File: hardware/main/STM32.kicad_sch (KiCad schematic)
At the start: 36 parts, among them U201 REF3430QDGKRQ1, U202 STM32L431RCTx

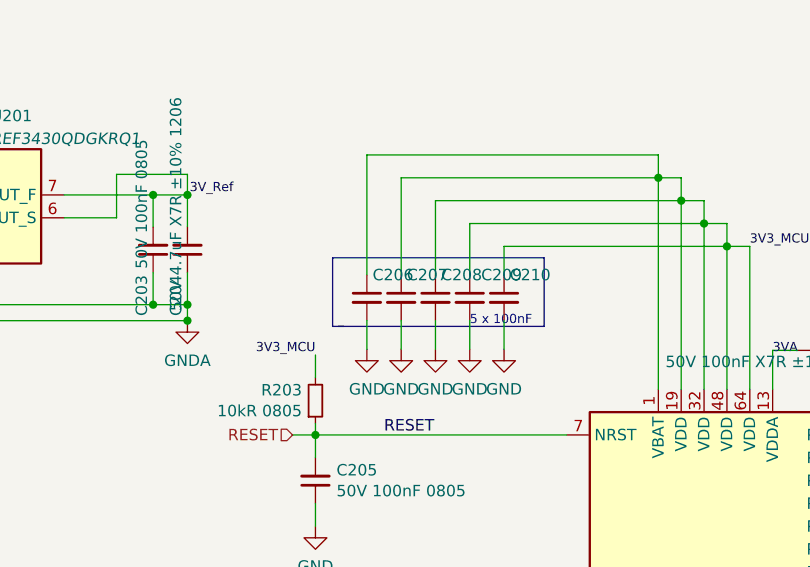
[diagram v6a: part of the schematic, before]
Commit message: Layout: Fist version of power stage
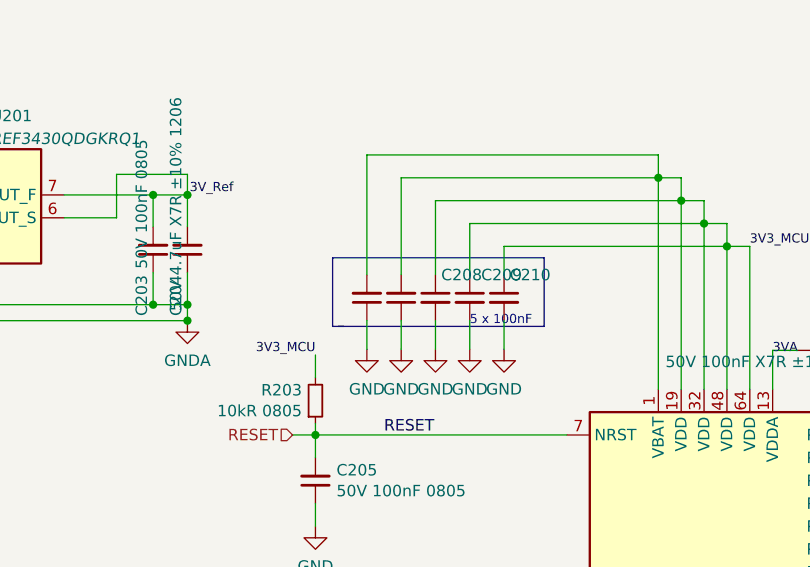
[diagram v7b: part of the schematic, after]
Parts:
- C206, C207: value 50V 100nF X7R ±10% 0402 -> 50V 100nF 0805; footprint Capacitor_SMD:C_0402_1005Metric_Pad0.74x0.62mm_HandSolder -> Capacitor_SMD:C_0805_2012Metric_Pad1.18x1.45mm_HandSolder
- JP201, JP202, JP204, JP205, JP206, JP207: footprint Jumper:SolderJumper-2_P1.3mm_Open_TrianglePad1.0x1.5mm -> Zenite:SolderJumper-2_P0.5mm_Open_TrianglePad0.5x0.5mm
- JP203: footprint Jumper:SolderJumper-3_P1.3mm_Open_Pad1.0x1.5mm -> Jumper:SolderJumper-3_P2.0mm_Open_TrianglePad1.0x1.5mm
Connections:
- net 3V3_MCU: now also C206.2, C207.2; no longer C206.1, C207.1
- net GND: now also C206.1, C207.1; no longer C206.2, C207.2
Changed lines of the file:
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@@
       (effects (font (size 1 1)))
     )
-    (property "Footprint" "Jumper:SolderJumper-2_P1.3mm_Open_TrianglePad1.0x1.5mm" (id 2) (at 167.64 142.24 0)
+    (property "Footprint" "Zenite:SolderJumper-2_P0.5mm_Open_TrianglePad0.5x0.5mm" (id 2) (at 167.64 142.24 0)
       (effects (font (size 1.27 1.27)) hide)
     )
@@
     (property "Reference" "JP202" (id 0) (at 241.3 18.5252 0))
     (property "Value" "Enable Voltage Reference" (id 1) (at 241.3 21.0621 0))
-    (property "Footprint" "Jumper:SolderJumper-2_P1.3mm_Open_TrianglePad1.0x1.5mm" (id 2) (at 241.3 22.86 0)
+    (property "Footprint" "Zenite:SolderJumper-2_P0.5mm_Open_TrianglePad0.5x0.5mm" (id 2) (at 241.3 22.86 0)
       (effects (font (size 1.27 1.27)) hide)
     )
     (property "Datasheet" "~" (id 3) (at 241.3 22.86 0)
-      (effects (font (size 1.27 1.27)) hide)
-    )
-    (pin "1")
-    (pin "2")
-  )
-  (symbol (lib_id "Device:C_Small") (at 100.33 60.96 0) (unit 1)
-    (in_bom yes) (on_board yes)
-    (property "Reference" "C206" (id 0) (at 100.965 58.42 0)
-      (effects (font (size 1.27 1.27)) (justify left))
-    )
-    (property "Value" "50V 100nF X7R ±10% 0402" (id 1) (at 102.7811 62.6685 0)
-      (effects (font (size 1.27 1.27)) (justify left) hide)
-    )
-    (property "Footprint" "Capacitor_SMD:C_0402_1005Metric_Pad0.74x0.62mm_HandSolder" (id 2) (at 100.33 60.96 0)
-      (effects (font (size 1.27 1.27)) hide)
-    )
-    (property "Datasheet" "~" (id 3) (at 100.33 60.96 0)
       (effects (font (size 1.27 1.27)) hide)
     )
@@
     (property "Reference" "JP201" (id 0) (at 240.03 45.8302 0))
     (property "Value" "Enable Stm32 Supply" (id 1) (at 240.03 48.3671 0))
-    (property "Footprint" "Jumper:SolderJumper-2_P1.3mm_Open_TrianglePad1.0x1.5mm" (id 2) (at 240.03 50.165 0)
+    (property "Footprint" "Zenite:SolderJumper-2_P0.5mm_Open_TrianglePad0.5x0.5mm" (id 2) (at 240.03 50.165 0)
       (effects (font (size 1.27 1.27)) hide)
     )
@@
     )
     (property "Datasheet" "~" (id 3) (at 37.465 56.134 0)
+      (effects (font (size 1.27 1.27)) hide)
+    )
+    (pin "1")
+    (pin "2")
+  )
+  (symbol (lib_id "Device:C_Small") (at 104.14 60.96 180) (unit 1)
+    (in_bom yes) (on_board yes)
+    (property "Reference" "C207" (id 0) (at 106.4768 59.7916 0)
+      (effects (font (size 1.27 1.27)) (justify right) hide)
+    )
+    (property "Value" "50V 100nF 0805" (id 1) (at 106.4768 62.103 0)
+      (effects (font (size 1.27 1.27)) (justify right) hide)
+    )
+    (property "Footprint" "Capacitor_SMD:C_0805_2012Metric_Pad1.18x1.45mm_HandSolder" (id 2) (at 104.14 60.96 0)
+      (effects (font (size 1.27 1.27)) hide)
+    )
+    (property "Datasheet" "~" (id 3) (at 104.14 60.96 0)
       (effects (font (size 1.27 1.27)) hide)
     )
@@
     (pin "1")
   )
+  (symbol (lib_id "Device:C_Small") (at 100.33 60.96 180) (unit 1)
+    (in_bom yes) (on_board yes)
+    (property "Reference" "C206" (id 0) (at 102.6668 59.7916 0)
+      (effects (font (size 1.27 1.27)) (justify right) hide)
+    )
+    (property "Value" "50V 100nF 0805" (id 1) (at 102.6668 62.103 0)
+      (effects (font (size 1.27 1.27)) (justify right) hide)
+    )
+    (property "Footprint" "Capacitor_SMD:C_0805_2012Metric_Pad1.18x1.45mm_HandSolder" (id 2) (at 100.33 60.96 0)
+      (effects (font (size 1.27 1.27)) hide)
+    )
+    (property "Datasheet" "~" (id 3) (at 100.33 60.96 0)
+      (effects (font (size 1.27 1.27)) hide)
+    )
+    (pin "1")
+    (pin "2")
+  )
   (symbol (lib_id "power:GND") (at 205.74 165.735 0) (unit 1)
     (in_bom yes) (on_board yes) (fields_autoplaced)
@@
       (effects (font (size 1 1)))
     )
-    (property "Footprint" "Jumper:SolderJumper-2_P1.3mm_Open_TrianglePad1.0x1.5mm" (id 2) (at 167.64 137.16 0)
+    (property "Footprint" "Zenite:SolderJumper-2_P0.5mm_Open_TrianglePad0.5x0.5mm" (id 2) (at 167.64 137.16 0)
       (effects (font (size 1.27 1.27)) hide)
     )
@@
       (effects (font (size 1 1)))
     )
-    (property "Footprint" "Jumper:SolderJumper-2_P1.3mm_Open_TrianglePad1.0x1.5mm" (id 2) (at 167.64 139.7 0)
+    (property "Footprint" "Zenite:SolderJumper-2_P0.5mm_Open_TrianglePad0.5x0.5mm" (id 2) (at 167.64 139.7 0)
       (effects (font (size 1.27 1.27)) hide)
     )
@@
       (effects (font (size 1 1)))
     )
-    (property "Footprint" "Jumper:SolderJumper-2_P1.3mm_Open_TrianglePad1.0x1.5mm" (id 2) (at 167.64 134.62 0)
+    (property "Footprint" "Zenite:SolderJumper-2_P0.5mm_Open_TrianglePad0.5x0.5mm" (id 2) (at 167.64 134.62 0)
       (effects (font (size 1.27 1.27)) hide)
     )
@@
     (pin "1")
   )
-  (symbol (lib_id "Device:C_Small") (at 104.14 60.96 0) (unit 1)
-    (in_bom yes) (on_board yes)
-    (property "Reference" "C207" (id 0) (at 104.775 58.42 0)
-      (effects (font (size 1.27 1.27)) (justify left))
-    )
-    (property "Value" "50V 100nF X7R ±10% 0402" (id 1) (at 106.5911 62.6685 0)
-      (effects (font (size 1.27 1.27)) (justify left) hide)
-    )
-    (property "Footprint" "Capacitor_SMD:C_0402_1005Metric_Pad0.74x0.62mm_HandSolder" (id 2) (at 104.14 60.96 0)
-      (effects (font (size 1.27 1.27)) hide)
-    )
-    (property "Datasheet" "~" (id 3) (at 104.14 60.96 0)
-      (effects (font (size 1.27 1.27)) hide)
-    )
-    (pin "1")
-    (pin "2")
-  )
   (symbol (lib_id "Jumper:Jumper_3_Bridged12") (at 241.3 36.195 0) (unit 1)
     (in_bom yes) (on_board yes) (fields_autoplaced)
     (property "Reference" "JP203" (id 0) (at 241.3 31.631 0))
     (property "Value" "Analog_Ref" (id 1) (at 241.3 34.1679 0))
-    (property "Footprint" "Jumper:SolderJumper-3_P1.3mm_Open_Pad1.0x1.5mm" (id 2) (at 241.3 36.195 0)
-      (effects (font (size 1.27 1.27)) hide)
-    )
+    (property "Footprint" "Jumper:SolderJumper-3_P2.0mm_Open_TrianglePad1.0x1.5mm" (id 2) (at 241.3 36.195 0)
+      (effects (font (size 1.27 1.27)) hide)
+    )

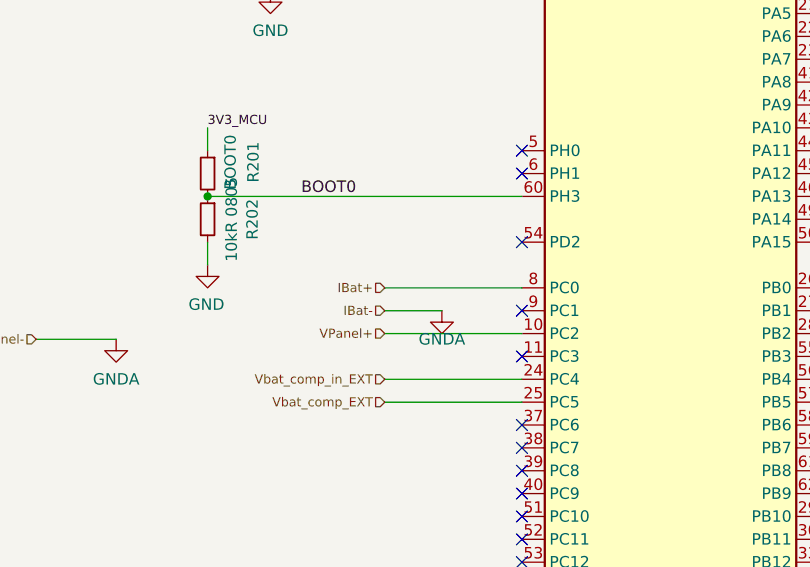
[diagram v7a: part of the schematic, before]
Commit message: Layout: Organize and initialize routing of control
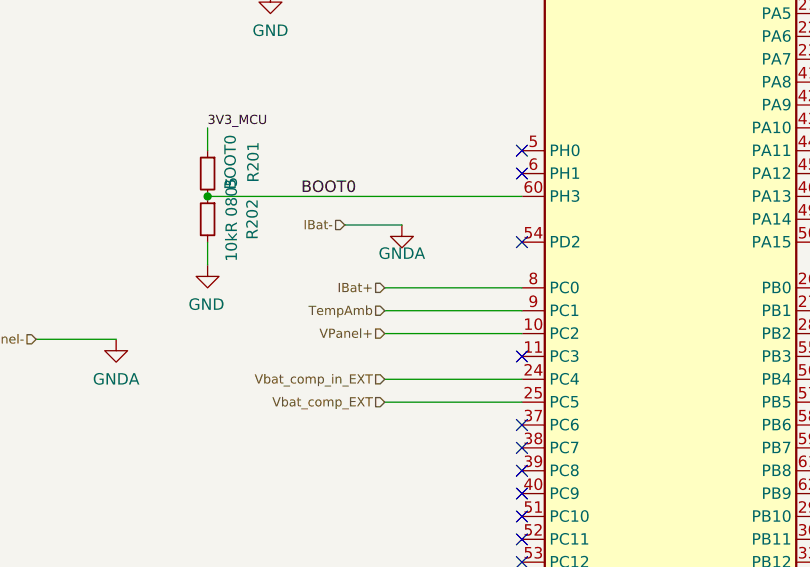
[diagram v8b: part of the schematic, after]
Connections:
- net TempAmb: now reaches U202.9 (PC1)
- no-connect marks 19 -> 18
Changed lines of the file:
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@@
   (junction (at 80.391 61.722) (diameter 0) (color 0 0 0 0)
   )
-  (no_connect (at 122.555 121.92))
   (no_connect (at 122.555 157.48))
   (no_connect (at 122.555 127))
@@
     (stroke (width 0) (type default) (color 0 0 0 0))
   )
-  (wire (pts (xy 107.315 121.92) (xy 113.665 121.92))
+  (wire (pts (xy 102.87 112.395) (xy 109.22 112.395))
     (stroke (width 0) (type default) (color 0 0 0 0))
   )
@@
   )
   (wire (pts (xy 239.395 154.94) (xy 239.395 158.75))
+    (stroke (width 0) (type default) (color 0 0 0 0))
+  )
+  (wire (pts (xy 107.315 121.92) (xy 122.555 121.92))
     (stroke (width 0) (type default) (color 0 0 0 0))
   )
@@
     (effects (font (size 1.016 1.016)) (justify left bottom))
   )
-  (hierarchical_label "IBat-" (shape input) (at 107.315 121.92 180)
+  (hierarchical_label "IBat-" (shape input) (at 102.87 112.395 180)
     (effects (font (size 1.016 1.016)) (justify right))
   )
@@
   (hierarchical_label "CAN_RX" (shape input) (at 167.005 104.14 0)
     (effects (font (size 1.27 1.27)) (justify left))
+  )
+  (hierarchical_label "TempAmb" (shape input) (at 107.315 121.92 180)
+    (effects (font (size 1.016 1.016)) (justify right))
   )
   (hierarchical_label "5V" (shape input) (at 232.41 22.86 180)
@@
     (pin "1")
   )
-  (symbol (lib_id "power:GNDA") (at 113.665 121.92 0) (unit 1)
+  (symbol (lib_id "power:GNDA") (at 109.22 112.395 0) (unit 1)
     (in_bom yes) (on_board yes)
-    (property "Reference" "#PWR0210" (id 0) (at 113.665 128.27 0)
-      (effects (font (size 1.27 1.27)) hide)
-    )
-    (property "Value" "GNDA" (id 1) (at 113.665 125.095 0))
-    (property "Footprint" "" (id 2) (at 113.665 121.92 0)
-      (effects (font (size 1.27 1.27)) hide)
-    )
-    (property "Datasheet" "" (id 3) (at 113.665 121.92 0)
-      (effects (font (size 1.27 1.27)) hide)
-    )
+    (property "Reference" "#PWR0210" (id 0) (at 109.22 118.745 0)
+      (effects (font (size 1.27 1.27)) hide)
+    )
+    (property "Value" "GNDA" (id 1) (at 109.22 115.57 0))
+    (property "Footprint" "" (id 2) (at 109.22 112.395 0)
+      (effects (font (size 1.27 1.27)) hide)
+    )
+    (property "Datasheet" "" (id 3) (at 109.22 112.395 0)
+      (effects (font (size 1.27 1.27)) hide)
+    )
